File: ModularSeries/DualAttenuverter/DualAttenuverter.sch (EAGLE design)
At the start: 33 parts, among them IC1 TL084P, P1 B10K, P2 B10K, U1 LM358

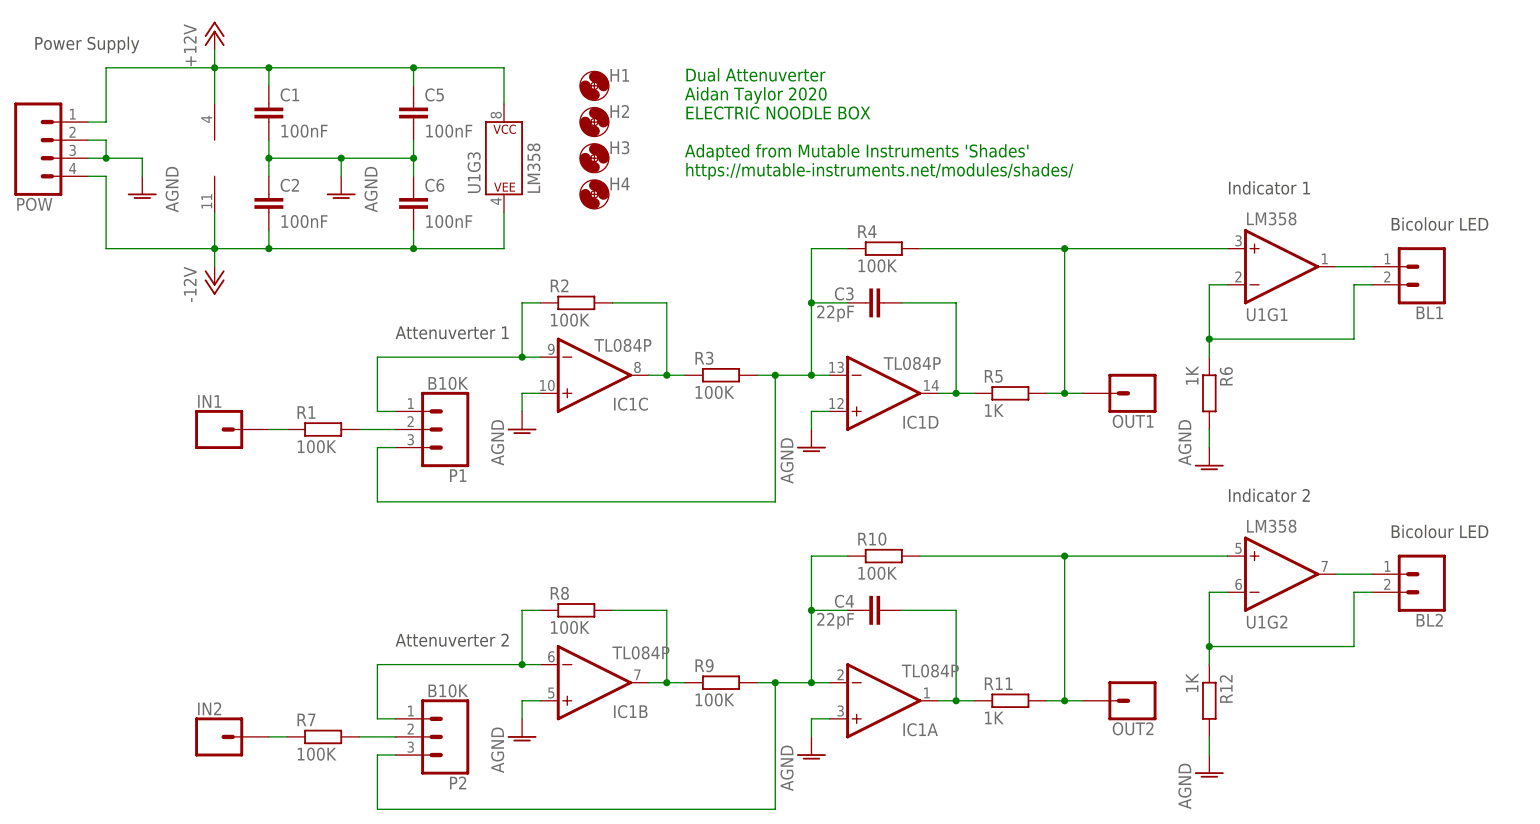
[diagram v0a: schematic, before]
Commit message: All PCBs now use unified library, Eagle library added
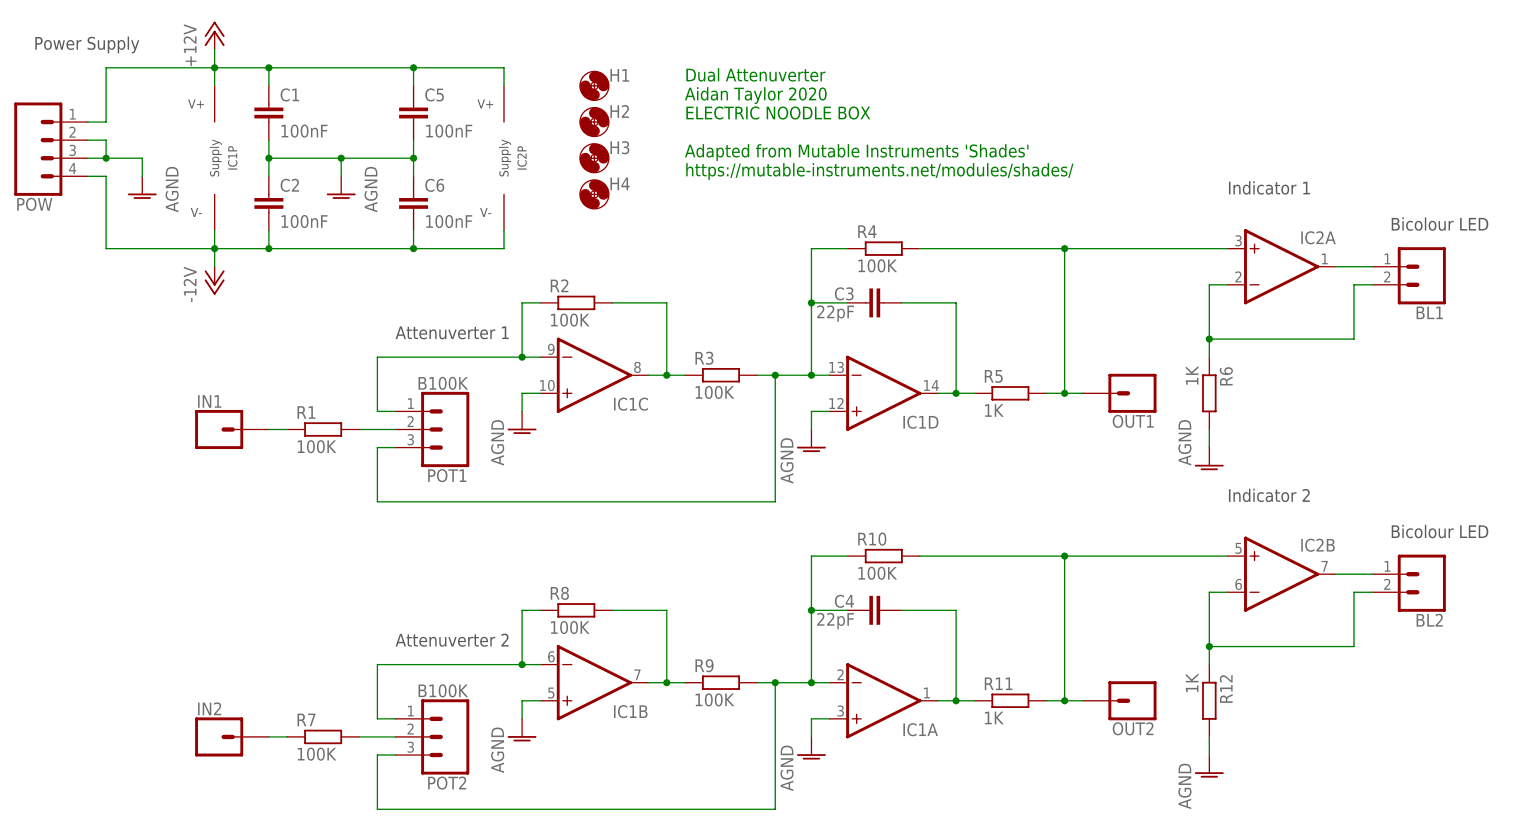
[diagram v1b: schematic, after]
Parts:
- removed P1, P2: B10K, SparkFun-Connectors:CONN_03
- removed U1: LM358, SparkFun-IC-Amplifiers:LM358
- added IC2: LM358_DIP, ElectricNoodleBox:LM358_DIP
- added POT1, POT2: B100K, ElectricNoodleBox:3XWIREPAD
- BL1, BL2: value (none) -> 2XWIREPAD; device SparkFun-Connectors:CONN_02 -> ElectricNoodleBox:2XWIREPAD
- IC1: value TL084P -> TL0X4_DIP; device linear:TL084P -> ElectricNoodleBox:TL0X4_DIP
- IN1, IN2, OUT1, OUT2: value (none) -> 1XWIREPAD; device SparkFun-Connectors:CONN_01 -> ElectricNoodleBox:1XWIREPAD
- POW: value (none) -> 4XMOLEX; device SparkFun-Connectors:CONN_04POLAR -> ElectricNoodleBox:4XMOLEX
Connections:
- removed net N$10: P2.2, R7.2
- new net N$3: POT2.2, R7.2
- net +12V: now also IC2P.V+; no longer U1G3.P$V+
- net -12V: now also IC2P.V-; no longer U1G3.P$V-
- net N$1: now also POT1.2; no longer P1.2
- net N$11: now also POT2.1; no longer P2.1
- net N$13: now also POT2.3; no longer P2.3
- net N$14: now also IC2B.+IN; no longer U1G2.+IN
- net N$17: now also IC2B.OUT; no longer U1G2.OUT
- net N$18: now also IC2B.-IN; no longer U1G2.-IN
- net N$19: now also IC2A.-IN; no longer U1G1.-IN
- net N$2: now also POT1.1; no longer P1.1
- net N$5: now also POT1.3; no longer P1.3
- net N$6: now also IC2A.+IN; no longer U1G1.+IN
- net N$8: now also IC2A.OUT; no longer U1G1.OUT

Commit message: Library updated, variants consolidated
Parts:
- IC1: value TL0X4_DIP -> (none); device ElectricNoodleBox:TL0X4_DIP -> ElectricNoodleBox:TL0X4DIL
- IC2: value LM358_DIP -> LM358; device ElectricNoodleBox:LM358_DIP -> ElectricNoodleBox:LM358
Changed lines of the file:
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@@
 </classes>
 <parts>
-<part name="IC1" library="ElectricNoodleBox" deviceset="TL0X4_DIP" device="" package3d_urn="urn:adsk.eagle:package:16407/2"/>
+<part name="IC1" library="ElectricNoodleBox" deviceset="TL0X4" device="DIL" package3d_urn="urn:adsk.eagle:package:16407/2"/>
 <part name="R1" library="rcl" library_urn="urn:adsk.eagle:library:334" deviceset="R-EU_" device="0207/10" package3d_urn="urn:adsk.eagle:package:23491/2" value="100K"/>
 <part name="C1" library="rcl" library_urn="urn:adsk.eagle:library:334" deviceset="C-EU" device="050-025X075" package3d_urn="urn:adsk.eagle:package:23637/1" value="100nF"/>
@@
 <part name="POT1" library="ElectricNoodleBox" deviceset="3XWIREPAD" device="" value="B100K"/>
 <part name="POT2" library="ElectricNoodleBox" deviceset="3XWIREPAD" device="" value="B100K"/>
-<part name="IC2" library="ElectricNoodleBox" deviceset="LM358_DIP" device="" package3d_urn="urn:adsk.eagle:package:29519/2"/>
+<part name="IC2" library="ElectricNoodleBox" deviceset="LM358" device="" package3d_urn="urn:adsk.eagle:package:29519/2"/>
 </parts>
 <sheets>
